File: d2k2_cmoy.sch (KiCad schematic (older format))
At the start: 6 parts

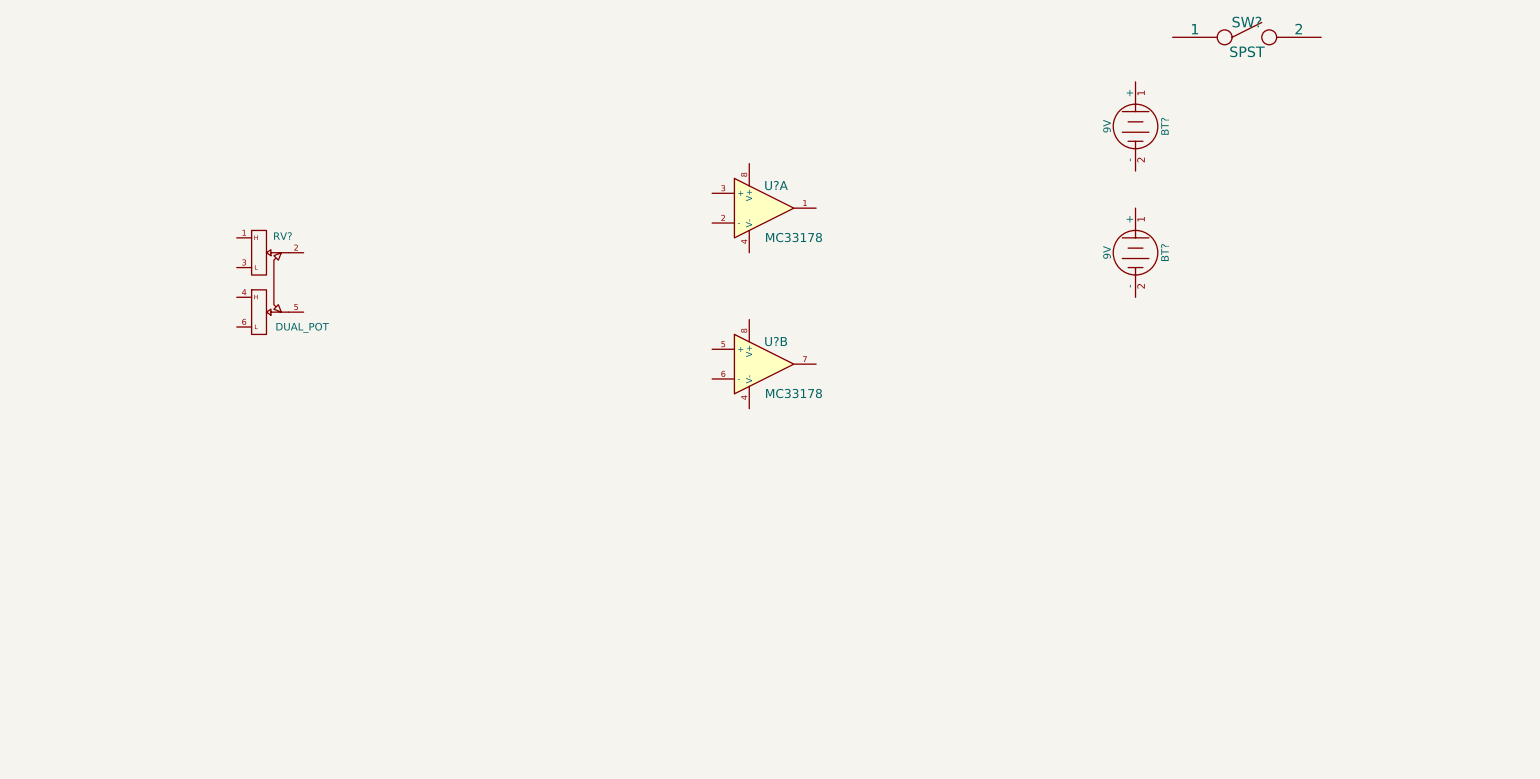
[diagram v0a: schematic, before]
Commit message: Basic cmoy design finished
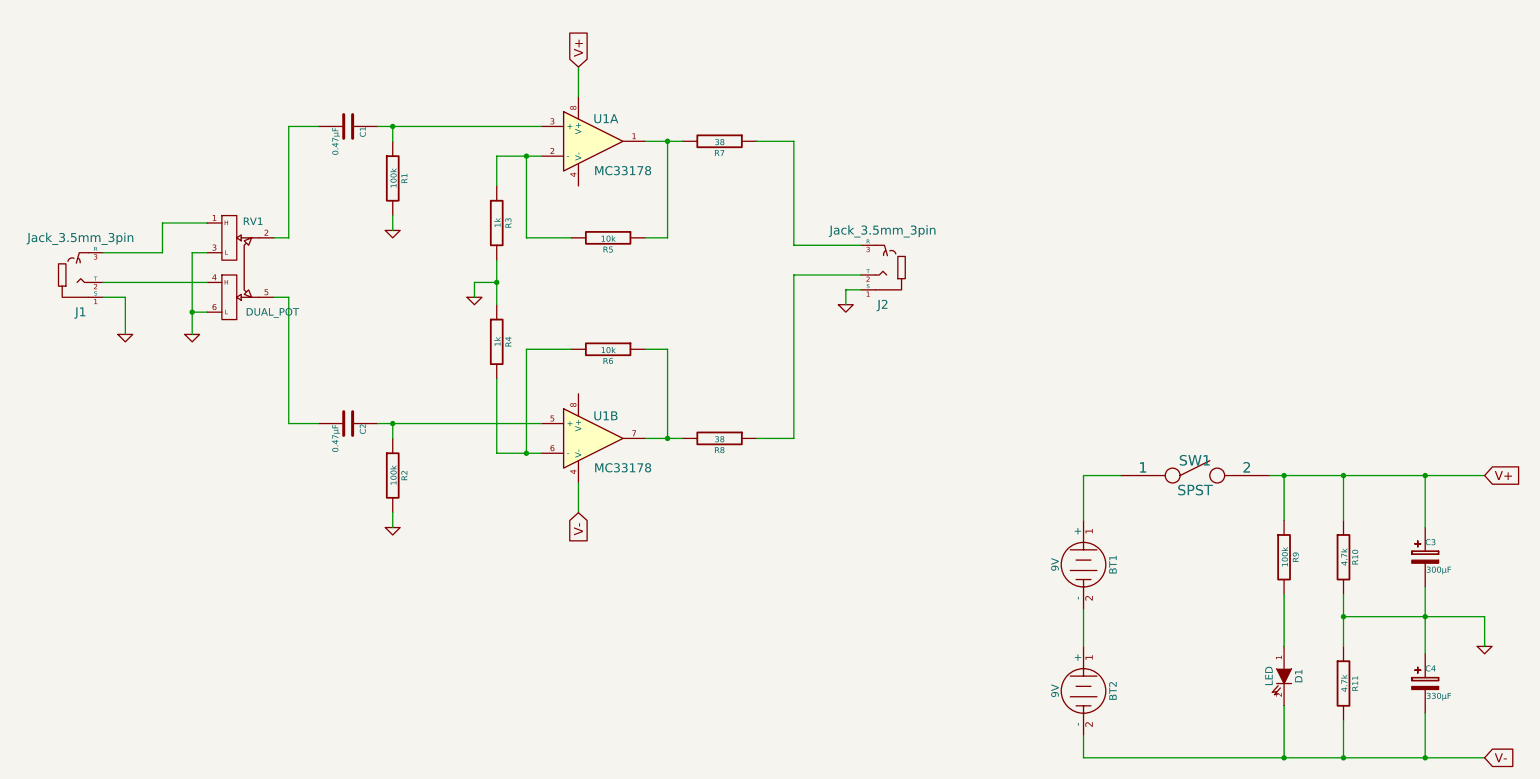
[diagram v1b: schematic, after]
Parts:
- added C1, C2: 0.47µF, symbol C
- added C3: 300µF, symbol CP2
- added C4: 330µF, symbol CP2
- added D1: LED, symbol LED
- added J1, J2: Jack_3.5mm_3pin, symbol Jack_3.5mm_3pin
- added R1, R2, R9: 100k, symbol R
- added R10, R11: 4.7k, symbol R
- added R3, R4: 1k, symbol R
- added R5, R6: 10k, symbol R
- added R7, R8: 38, symbol R
- gave numbers to parts that had none: 5
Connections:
- net at BT1.1 (+): now also SW1.1
- net at BT1.2 (-): now also BT2.1 (+)
- net V-: now reaches BT2.2 (-)
- net V-: now also U1.4 (V-), C4.2, D1.2 (K), R11.2
- net V+: now reaches SW1.2
- net V+: now also U1.8 (V+), C3.1, R10.1, R9.1
- net at U1.1: now also R5.1, R7.2
- net at U1.2 (-): now also R3.1, R5.2
- net at U1.3 (+): now also C1.1, R1.1
- net at U1.5 (+): now also C2.1, R2.1
- net at U1.6 (-): now also R4.2, R6.2
- net at U1.7: now also R6.1, R8.2
- net at RV1.1: now also J1.3 (R)
- net at RV1.2: now also C1.2
- net GND: now reaches RV1.3
- net GND: now also RV1.6, C3.2, C4.1, J1.1 (S), J2.1 (S), R1.2, R10.2, R11.1, R2.2, R3.2, R4.1
- net at RV1.4: now also J1.2 (T)
- net at RV1.5: now also C2.2
- new net: J2.2 (T), R8.1
- new net: J2.3 (R), R7.1
- new net: D1.1 (A), R9.2
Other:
- moved on the sheet: BT1, BT2, RV1, SW1, U1A, U1B
